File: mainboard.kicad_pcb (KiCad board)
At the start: 2 copper layers, 10 parts, among them J1 105017-1001, J2 XT60-M, U1 ESP32-WROOM-32E_(16MB), U2 CH340E, U3 AMS1117-3.3

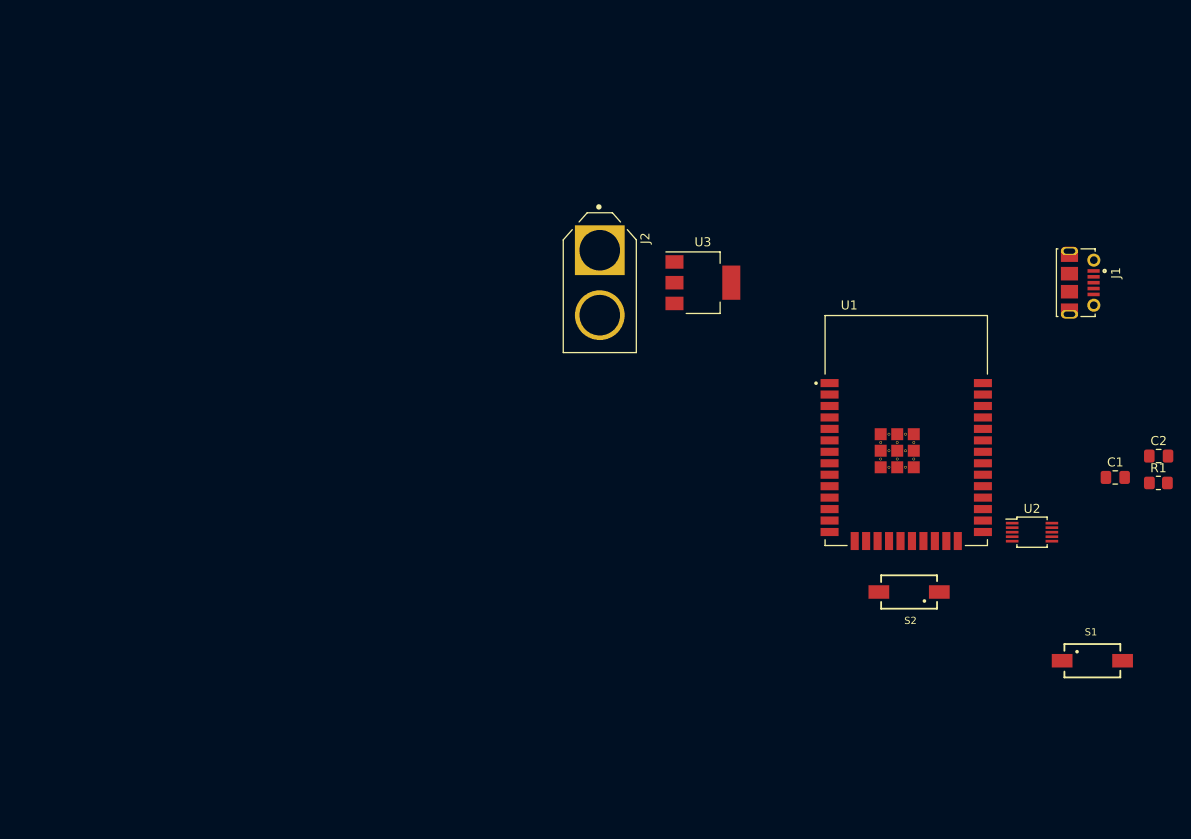
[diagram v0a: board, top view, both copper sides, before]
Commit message: update
toevoegen mosfet en versterker in schematic
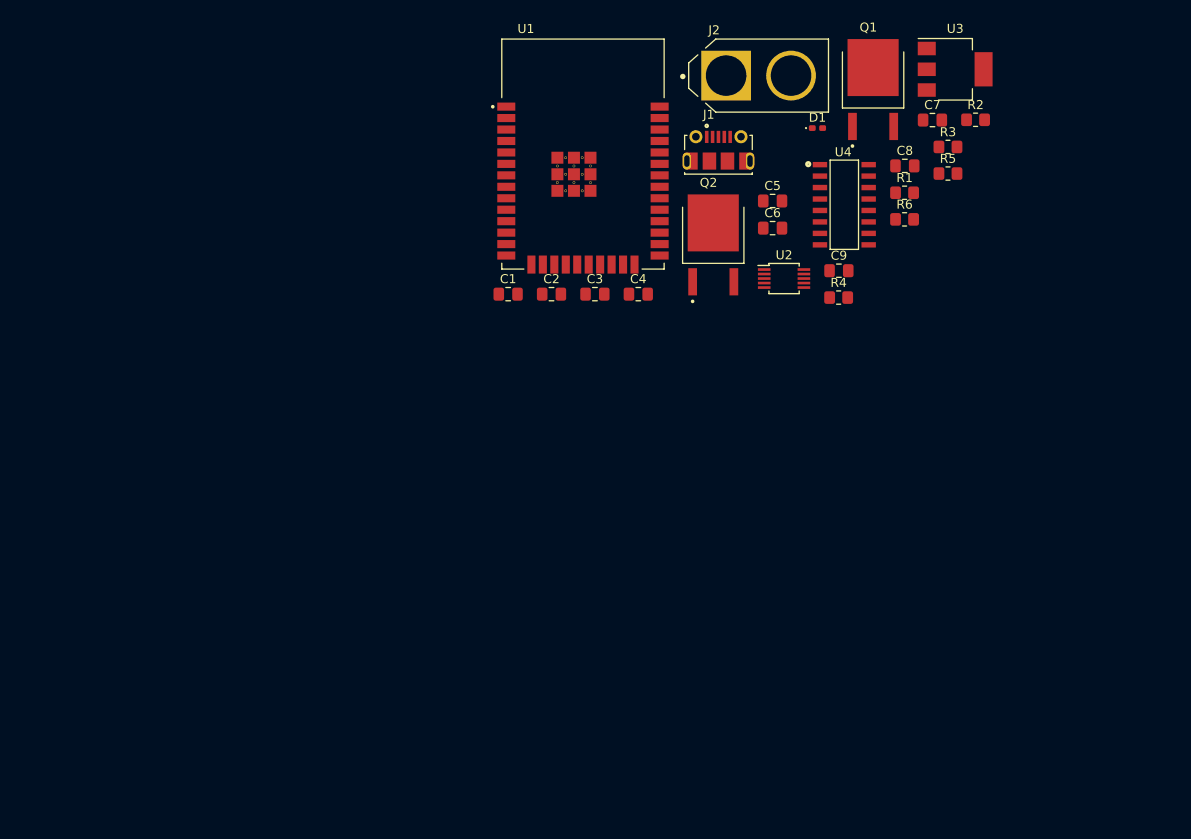
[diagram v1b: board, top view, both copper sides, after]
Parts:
- removed S1: EN, 434111043826:434111043826
- removed S2: BOOT, 434111043826:434111043826
- added C3: C, Capacitor_SMD:C_0805_2012Metric_Pad1.18x1.45mm_HandSolder, F.Cu at (102.3, 78.7)
- added C4: C, Capacitor_SMD:C_0805_2012Metric_Pad1.18x1.45mm_HandSolder, F.Cu at (107.1, 78.7)
- added C5: C, Capacitor_SMD:C_0805_2012Metric_Pad1.18x1.45mm_HandSolder, F.Cu at (122.0, 68.4)
- added C6: C, Capacitor_SMD:C_0805_2012Metric_Pad1.18x1.45mm_HandSolder, F.Cu at (122.0, 71.4)
- added C7: C, Capacitor_SMD:C_0805_2012Metric_Pad1.18x1.45mm_HandSolder, F.Cu at (139.8, 59.4)
- added C8: C, Capacitor_SMD:C_0805_2012Metric_Pad1.18x1.45mm_HandSolder, F.Cu at (136.7, 64.5)
- added C9: C, Capacitor_SMD:C_0805_2012Metric_Pad1.18x1.45mm_HandSolder, F.Cu at (129.4, 76.1)
- added D1: D, Diode_SMD:D_0402_1005Metric_Pad0.77x0.64mm_HandSolder, F.Cu at (127.0, 60.3)
- added Q1: AOD4184A, mylibs:DPAK228P994X240-4N, F.Cu at (133.2, 56.1)
- added Q2: AOD4184A, mylibs:DPAK228P994X240-4N, F.Cu at (115.5, 73.3)
- added R2: R, Resistor_SMD:R_0805_2012Metric_Pad1.20x1.40mm_HandSolder, F.Cu at (144.5, 59.4)
- added R3: R, Resistor_SMD:R_0805_2012Metric_Pad1.20x1.40mm_HandSolder, F.Cu at (141.5, 62.4)
- added R4: R, Resistor_SMD:R_0805_2012Metric_Pad1.20x1.40mm_HandSolder, F.Cu at (129.3, 79.1)
- added R5: R, Resistor_SMD:R_0805_2012Metric_Pad1.20x1.40mm_HandSolder, F.Cu at (141.5, 65.4)
- added R6: R, Resistor_SMD:R_0805_2012Metric_Pad1.20x1.40mm_HandSolder, F.Cu at (136.7, 70.5)
- added U4: PAM8403DR, mylibs:SOIC127P605X150-16N, F.Cu at (130.0, 68.8)
- moved C1 70.3 mm to (92.7, 78.7)
- moved C2 69.7 mm to (97.5, 78.7)
- moved U1 47.2 mm to (101.0, 63.2)
- moved R1 42.7 mm to (136.7, 67.5)
- moved J1 41.2 mm to (116.0, 64.0), turned to 0 degrees
- moved U2 39.3 mm to (123.3, 77.0)
- moved U3 36.6 mm to (142.3, 53.8)
- moved J2 28.9 mm to (120.5, 54.5), turned to 0 degrees
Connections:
- net GND renamed 5V

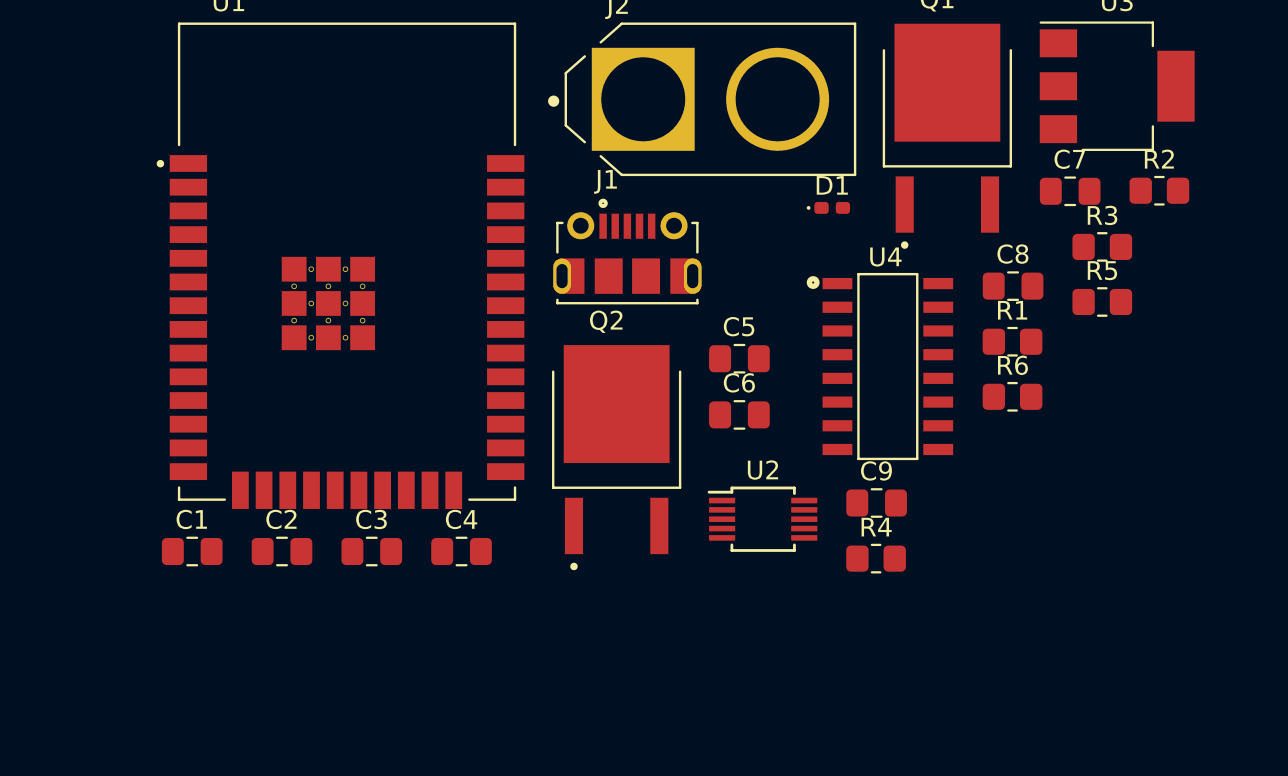
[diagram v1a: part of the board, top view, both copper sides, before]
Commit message: condensator toegevoegd aan ldo
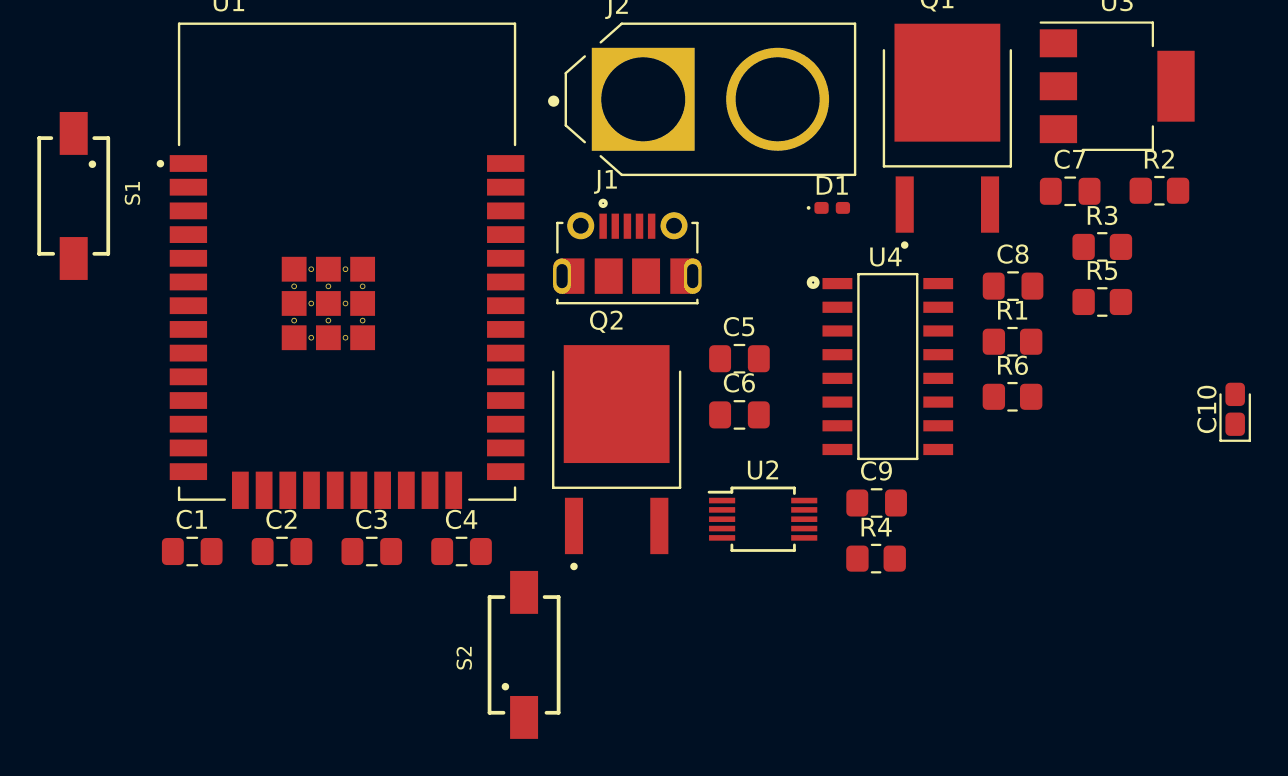
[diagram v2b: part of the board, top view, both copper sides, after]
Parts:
- added C10: CP, Capacitor_Tantalum_SMD:CP_EIA-1608-08_AVX-J_Pad1.25x1.05mm_HandSolder, F.Cu at (148.6, 71.1)
- added S1: EN, 434111043826:434111043826, F.Cu at (86.4, 59.7)
- added S2: BOOT, 434111043826:434111043826, F.Cu at (110.5, 84.3)
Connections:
- C1 pad 2: 5V -> GND
- C5 pad 2: 5V -> GND
- C6 pad 1: 5V -> GND
- C6 pad 2: Net-(C6-Pad2) -> 5V
- C7 pad 2: 5V -> GND
- C8 pad 2: 5V -> GND
- C9 pad 2: 5V -> GND
- D1 pad 1: 5V -> GND
- J1 pad 5: 5V -> GND
- J1 pad S1: 5V -> GND
- J1 pad S2: 5V -> GND
- J1 pad S3: 5V -> GND
- J1 pad S4: 5V -> GND
- J1 pad S5: 5V -> GND
- J1 pad S6: 5V -> GND
- J2 pad 1: 5V -> GND
- Q1 pad 3: 5V -> GND
- Q2 pad 3: 5V -> GND
- R5 pad 2: 5V -> GND
- U1 pad 1: 5V -> GND
- U1 pad 15: 5V -> GND
- U1 pad 38: 5V -> GND
- U1 pad 39_1: 5V -> GND
- U1 pad 39_10: 5V -> GND
- U1 pad 39_11: 5V -> GND
- U1 pad 39_12: 5V -> GND
- U1 pad 39_13: 5V -> GND
- U1 pad 39_14: 5V -> GND
- U1 pad 39_15: 5V -> GND
- U1 pad 39_16: 5V -> GND
- U1 pad 39_17: 5V -> GND
- U1 pad 39_18: 5V -> GND
- U1 pad 39_19: 5V -> GND
- U1 pad 39_2: 5V -> GND
- U1 pad 39_20: 5V -> GND
- U1 pad 39_21: 5V -> GND
- U1 pad 39_3: 5V -> GND
- U1 pad 39_4: 5V -> GND
- U1 pad 39_5: 5V -> GND
- U1 pad 39_6: 5V -> GND
- U1 pad 39_7: 5V -> GND
- U1 pad 39_8: 5V -> GND
- U1 pad 39_9: 5V -> GND
- U2 pad 3: 5V -> GND
- U3 pad 1: 5V -> GND
- U4 pad 11: 5V -> GND
- U4 pad 15: 5V -> GND
- U4 pad 2: 5V -> GND
- U4 pad 6: Net-(C6-Pad2) -> 5V

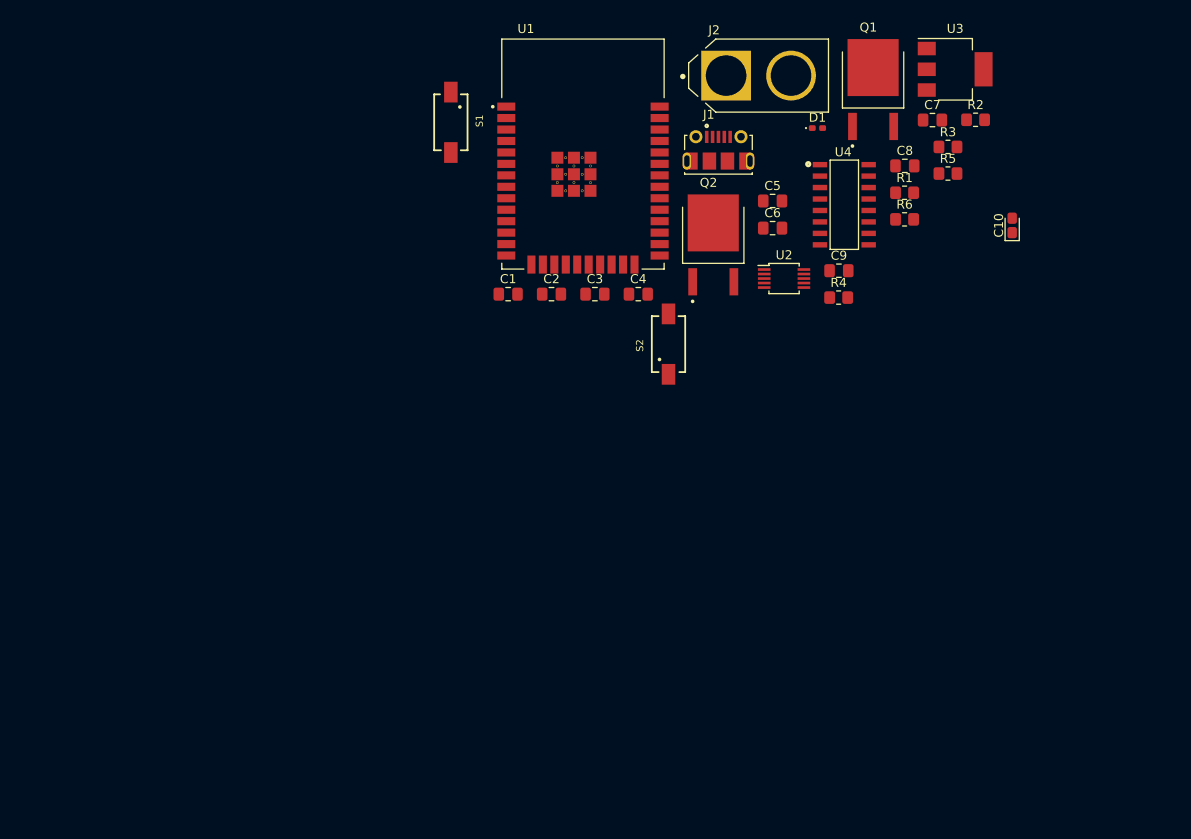
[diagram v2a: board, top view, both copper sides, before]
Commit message: ordenen pcb
kheb wa plek vrijgelaten voor de io pinnen
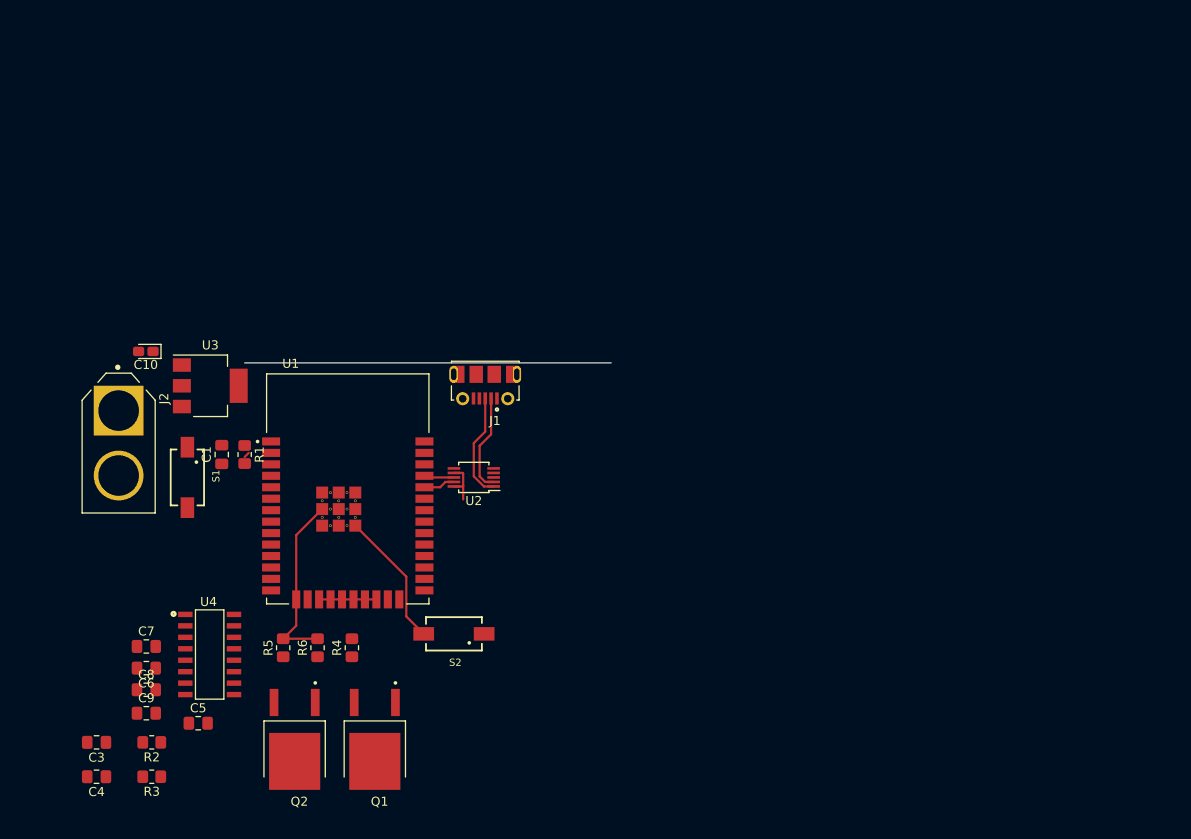
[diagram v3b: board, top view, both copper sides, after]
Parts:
- removed C2: C, Capacitor_SMD:C_0805_2012Metric_Pad1.18x1.45mm_HandSolder
- removed D1: D, Diode_SMD:D_0402_1005Metric_Pad0.77x0.64mm_HandSolder
- moved R2 114.5 mm to (53.2, 128.4), turned to 180 degrees
- moved R3 112.5 mm to (53.2, 132.2), turned to 180 degrees
- moved C7 104.9 mm to (52.6, 117.8)
- moved C8 102.2 mm to (52.6, 122.6)
- moved C10 97.1 mm to (52.5, 85.1), turned to 180 degrees
- moved C9 91.1 mm to (52.6, 125.2)
- moved Q1 90.8 mm to (77.9, 128.1), turned to 180 degrees
- moved R5 90.5 mm to (67.8, 117.9), turned to 90 degrees
- moved U3 89.7 mm to (59.7, 88.9)
- moved U4 86.2 mm to (59.6, 118.7)
- moved C5 86.1 mm to (58.4, 126.3)
- moved C6 84.9 mm to (52.6, 120.2), turned to 180 degrees
- moved J2 81.8 mm to (49.5, 95.2), turned to 270 degrees
- moved R6 80.6 mm to (71.6, 117.9), turned to 90 degrees
- moved C4 80.4 mm to (47.1, 132.2), turned to 180 degrees
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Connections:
- J1 pad 1: Net-(C2-Pad1) -> Net-(J1-Pad1)
- R6 pad 2: Net-(D1-Pad2) -> GND
- U1 pad 2: Net-(U1-Pad2) -> 3V3
- U1 pad 24: Net-(U1-Pad24) -> Mosfet_Trig
- U2 pad 10: Net-(C2-Pad2) -> 3V3
- U2 pad 7: Net-(C2-Pad1) -> 3V3
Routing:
- net GND: track 0.00 -> 35.1 mm
- net Net-(J1-Pad3): track 0.00 -> 11.8 mm
- net Net-(J1-Pad2): track 0.00 -> 11.0 mm
- net Net-(U1-Pad17): track 0.00 -> 6.35 mm
- net 3V3: track 0.00 -> 5.62 mm
- net RXD: track 0.00 -> 3.51 mm
- net TXD: track 0.00 -> 3.34 mm
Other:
- board text added: "PWM"
- board text added: "belangrijke IO pinnen"

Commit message: sorry stef
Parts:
- moved C9 10.5 mm to (42.4, 122.5), turned to 90 degrees
- moved U4 7.73 mm to (58.4, 126.3)
- moved C8 7.56 mm to (45.0, 122.5), turned to 90 degrees
- moved C5 7.05 mm to (58.7, 133.3)
- moved C6 5.63 mm to (47.4, 122.5), turned to 270 degrees
- moved C7 5.41 mm to (49.8, 122.5), turned to 90 degrees
- moved S1 5.24 mm to (52.1, 100.3)
- moved J2 5.08 mm to (44.5, 95.2), turned to 90 degrees
- moved S2 4.26 mm to (86.4, 120.7), turned to 270 degrees
- moved C10 3.84 mm to (52.1, 88.9), turned to 90 degrees
- moved U3 3.63 mm to (59.0, 92.5)
- moved C3 2.54 mm to (44.5, 128.4)
- moved C4 2.54 mm to (44.5, 132.2)
- moved R2 2.54 mm to (50.7, 128.4)
- moved R3 2.54 mm to (50.7, 132.2)
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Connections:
- net mute renamed Net-(U4-Pad5)
- U1 pad 14: Net-(U1-Pad14) -> SHND
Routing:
- net GND: track 35.1 -> 165.5 mm
- net 3V3: track 5.62 -> 49.5 mm, vias 0 -> 2
- net Net-(C1-Pad1): track 0.00 -> 16.9 mm
- net Net-(U1-Pad36): track 0.00 -> 15.5 mm
- net 5V: track 0.00 -> 14.1 mm
- net Net-(J2-Pad2): track 0.00 -> 12.7 mm
- net Net-(U1-Pad33): track 0.00 -> 11.4 mm
- net Net-(R2-Pad1): track 0.00 -> 4.43 mm
- net Net-(C4-Pad1): track 0.00 -> 4.08 mm
- net Net-(C3-Pad1): track 0.00 -> 4.08 mm
- net Net-(S2-Pad1): track 0.00 -> 0.77 mm
- net SHND: track 0.00 -> 0.55 mm
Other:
- board outline added: 64.8 x 50.8 mm
- board text added: "Ruimte voor connectors"
